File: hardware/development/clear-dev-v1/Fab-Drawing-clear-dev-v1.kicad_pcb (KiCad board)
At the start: 2 copper layers, 76.2 x 73.8 mm, 86 parts, among them J1 USB_B_Micro, J10 Conn_01x28_Pin, J11 Conn_01x28_Pin, J12 Conn_01x02_Pin, J2 Conn_01x02_Pin, J3 Conn_01x02_Pin, J4 Conn_01x03_Pin, J5 Conn_01x02_Pin, J6 Conn_01x02_Pin, J7 Conn_01x06_Pin, J8 Conn_01x02_Pin, J9 Conn_01x02_Pin, SW1 SW_Push - SKQGADE010, T1 Logo, T2 Logo, U1 FT232H, U10 DS1086LU, U2 SN74LVC1G125DCKR, U3 SN74LVC1G125DCKR, U4 SN74LVC1G125DCKR, U5 TAR5SxxU, U6 TAR5SxxU, U7 W25Q32FVSS, U8 M.2-CONNECTOR-E, U9 TMUX4053-BQB, X1 DSC6001_10MHZ, Y1 12MHz

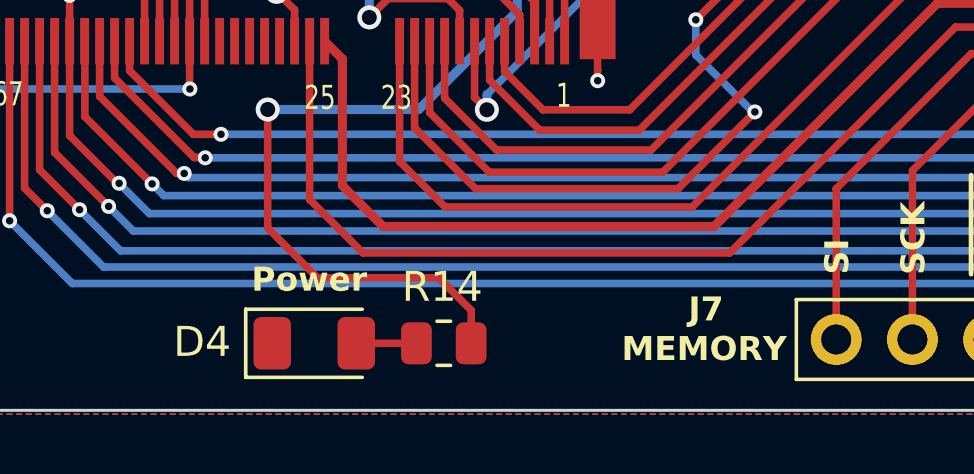
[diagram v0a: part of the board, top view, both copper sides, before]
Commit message: update clear board REV 1B
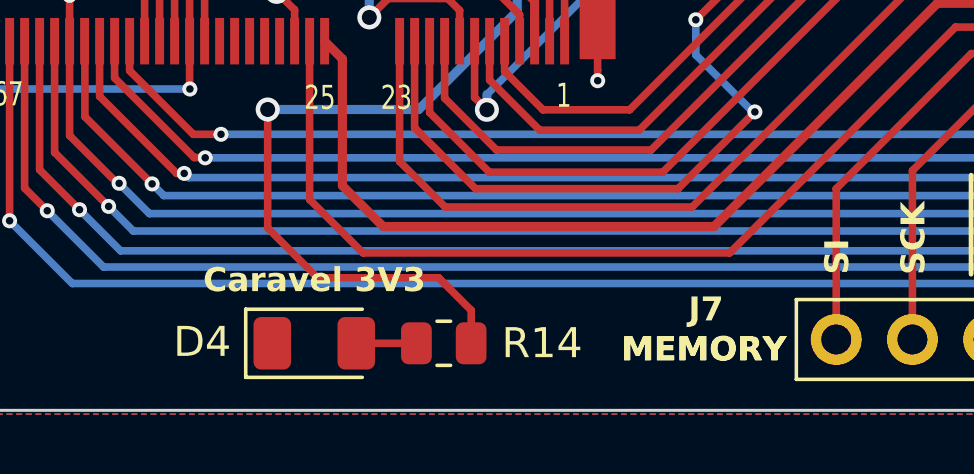
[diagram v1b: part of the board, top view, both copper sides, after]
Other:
- board text added: "Caravel 3V3"
- board text removed: "Power"
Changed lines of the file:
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@@
     (property "ki_keywords" "R res resistor")
     (attr smd)
-    (fp_text reference "R14" (at 0.0508 1.8796) (layer "F.SilkS")
+    (fp_text reference "R14" (at -3.2768 0) (layer "F.SilkS")
         (effects (font (size 1 1) (thickness 0.15)))
     )
@@
     (effects (font (size 0.8 0.8) (thickness 0.15) bold))
   )
-  (gr_text "Power" (at 122.8214 187.158) (layer "F.SilkS" knockout)
-    (effects (font (size 0.8 0.8) (thickness 0.16) bold))
-  )
   (gr_text "OSC ~{EN}" (at 153.9442 155.388) (layer "F.SilkS" knockout)
     (effects (font (size 0.8 0.8) (thickness 0.15) bold))
@@
     (effects (font (size 1 1) (thickness 0.2) bold))
   )
+  (gr_text "Caravel 3V3" (at 122.9912 187.1712) (layer "F.SilkS" knockout)
+    (effects (font (size 0.8 0.8) (thickness 0.16) bold))
+  )
   (gr_text "IO[23]" (at 101.1042 163.198) (layer "F.SilkS" knockout)
     (effects (font (size 1 1) (thickness 0.2) bold))
@@
     (effects (font (size 1 1) (thickness 0.15)))
   )
+  (gr_text "MEMORY" (at 135.9662 189.484) (layer "F.SilkS" knockout)
+    (effects (font (size 0.8 0.8) (thickness 0.16) bold))
+  )
   (gr_text "1\n" (at 155.1342 134.458 90) (layer "F.SilkS")
